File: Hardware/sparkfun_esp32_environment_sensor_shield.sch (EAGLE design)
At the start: 49 parts, among them J1 WEATHER_METER-WIND, J2 WEATHER_METER-RAIN, U1 BME280, U2 CCS811, U3 APDS-9301, U4 TVS Diode

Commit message: Feedback from review
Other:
- note added: "APDS-9301 - Luminosity (Lux)"
- note added: "APDS-9301 ===== VDD Range: 2.7-3.6V Max Current: 0.6mA"
- note added: "JP3 sets the I2C address of the APDS-9301 Open (both) - 0x51 High - 0x71 Low - 0x91"
- note removed: "JP3 sets the I2C address of the TSL2561 Open (both) - 0x39 High - 0x49 Low - 0x29"
- note removed: "TSL2561 - Luminosity (Lux)"
- note removed: "TSL2561 ===== VDD Range: 2.7-3.6V Max Current: 0.6mA"
- moved on the sheet: C6
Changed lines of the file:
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@@
 <sheet>
 <plain>
-<text x="104.14" y="119.38" size="1.27" layer="97">TSL2561
+<text x="104.14" y="119.38" size="1.27" layer="97">APDS-9301
 =====
 VDD Range: 2.7-3.6V
@@
 <wire x1="78.74" y1="76.2" x2="78.74" y2="132.08" width="0.254" layer="97" style="shortdash"/>
 <text x="0.762" y="131.318" size="2.54" layer="94" align="top-left">BME280 - Humidity, Pressure, Temp</text>
-<text x="79.502" y="131.318" size="2.54" layer="94" align="top-left">TSL2561 - Luminosity (Lux)</text>
+<text x="79.502" y="131.318" size="2.54" layer="94" align="top-left">APDS-9301 - Luminosity (Lux)</text>
 <text x="0.762" y="75.438" size="2.54" layer="94" align="top-left">Weather Meter - Rainfall, Wind Speed, Wind Direction</text>
 <wire x1="0" y1="25.4" x2="91.44" y2="25.4" width="0.254" layer="97" style="shortdash"/>
@@
 Closed - 0x76</text>
 <text x="81.28" y="81.28" size="1.27" layer="97" align="center-left">JP3 sets the I2C
-address of the TSL2561
-Open (both) - 0x39
-High - 0x49
-Low - 0x29</text>
+address of the APDS-9301
+Open (both) - 0x51
+High - 0x71
+Low - 0x91</text>
 <text x="111.76" y="157.48" size="1.27" layer="97" align="center-right">JP4 disconnects the on-
 board NTC thermistor,
@@
 <instance part="R14" gate="G$1" x="165.1" y="160.02" rot="R90"/>
 <instance part="SUPPLY18" gate="G$1" x="157.48" y="177.8"/>
-<instance part="C6" gate="G$1" x="139.7" y="116.84" rot="MR0"/>
-<instance part="SUPPLY17" gate="G$1" x="139.7" y="124.46"/>
-<instance part="GND15" gate="1" x="139.7" y="109.22"/>
+<instance part="C6" gate="G$1" x="139.7" y="114.3" rot="MR0"/>
+<instance part="SUPPLY17" gate="G$1" x="139.7" y="121.92"/>
+<instance part="GND15" gate="1" x="139.7" y="106.68"/>
 <instance part="SUPPLY1" gate="G$1" x="5.08" y="101.6"/>
 <instance part="R7" gate="G$1" x="91.44" y="111.76" rot="R90"/>
@@
 <pinref part="C6" gate="G$1" pin="2"/>
 <pinref part="GND15" gate="1" pin="GND"/>
-<wire x1="139.7" y1="111.76" x2="139.7" y2="114.3" width="0.1524" layer="91"/>
+<wire x1="139.7" y1="109.22" x2="139.7" y2="111.76" width="0.1524" layer="91"/>
 </segment>
 <segment>
@@
 <pinref part="C6" gate="G$1" pin="1"/>
 <pinref part="SUPPLY17" gate="G$1" pin="3.3V"/>
-<wire x1="139.7" y1="124.46" x2="139.7" y2="121.92" width="0.1524" layer="91"/>
-</segment>
-<segment>
+<wire x1="139.7" y1="121.92" x2="139.7" y2="119.38" width="0.1524" layer="91"/>
+</segment>
+<segment>

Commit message: Chg rev to 02
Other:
- note added: "02"
- note removed: "V01"
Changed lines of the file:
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@@
 to 4.7k pull-up
 resistors.</text>
-<text x="238.76" y="7.62" size="2.54" layer="94" align="center-left">V01</text>
+<text x="238.76" y="7.62" size="2.54" layer="94" align="center-left">02</text>
 <text x="170.18" y="7.62" size="2.54" layer="94" align="center-left">Jim Lindblom</text>
 <text x="119.38" y="20.32" size="1.27" layer="97" align="top-left">3-Pin temperature

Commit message: Fix issues from review
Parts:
- added FD3, FD4: FIDUCIAL1X2, SparkFun-Aesthetics:FIDUCIAL1X2
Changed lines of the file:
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@@
 <part name="LOGO3" library="SparkFun-Aesthetics" deviceset="SFE_LOGO_FLAME" device=".1_INCH"/>
 <part name="U3" library="SparkFun-Sensors" deviceset="APDS-9301" device="" value="APDS-9301"/>
+<part name="FD3" library="SparkFun-Aesthetics" deviceset="FIDUCIAL" device="1X2"/>
+<part name="FD4" library="SparkFun-Aesthetics" deviceset="FIDUCIAL" device="1X2"/>
 </parts>
 <sheets>
@@
 <instance part="LOGO3" gate="G$1" x="33.782" y="12.446"/>
 <instance part="U3" gate="G$1" x="116.84" y="99.06"/>
+<instance part="FD3" gate="G$1" x="236.22" y="27.94"/>
+<instance part="FD4" gate="G$1" x="236.22" y="25.4"/>
 </instances>
 <busses>

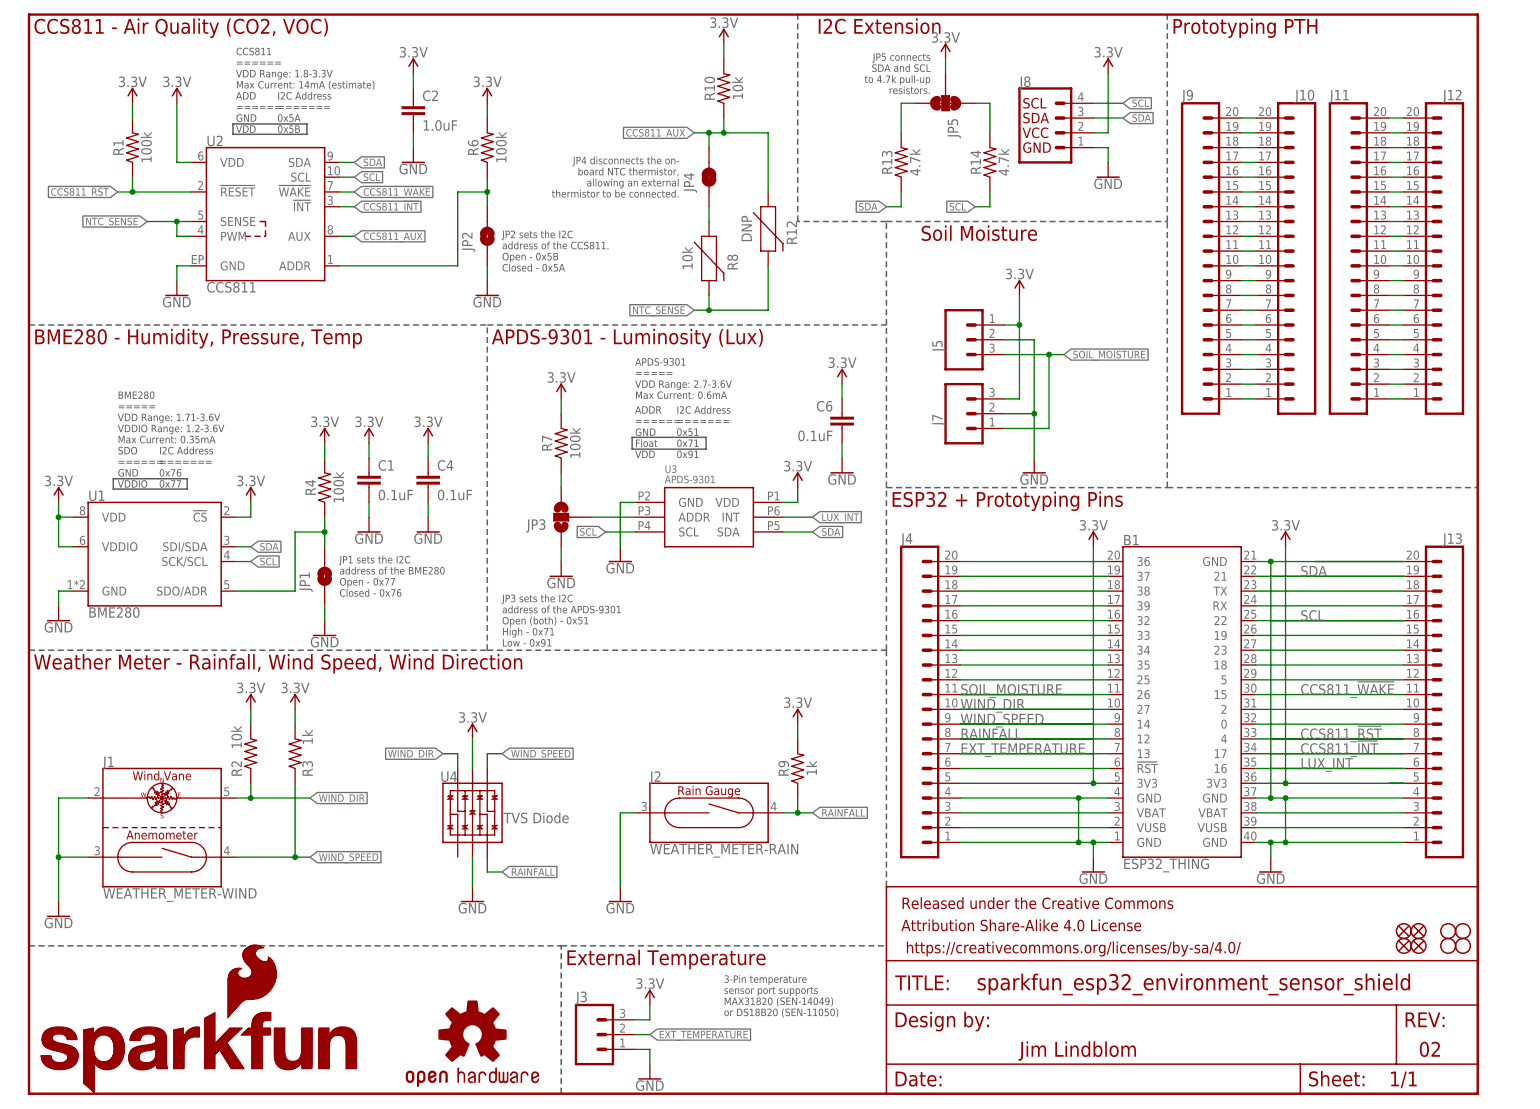
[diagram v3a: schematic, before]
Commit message: Changes after review of 02  - Change i2c addr info for apds-9301  - Change pin rain sensor is attached to  - Add debounce caps to rain sensor and anemometer  - Fix APDS-9301 footprint
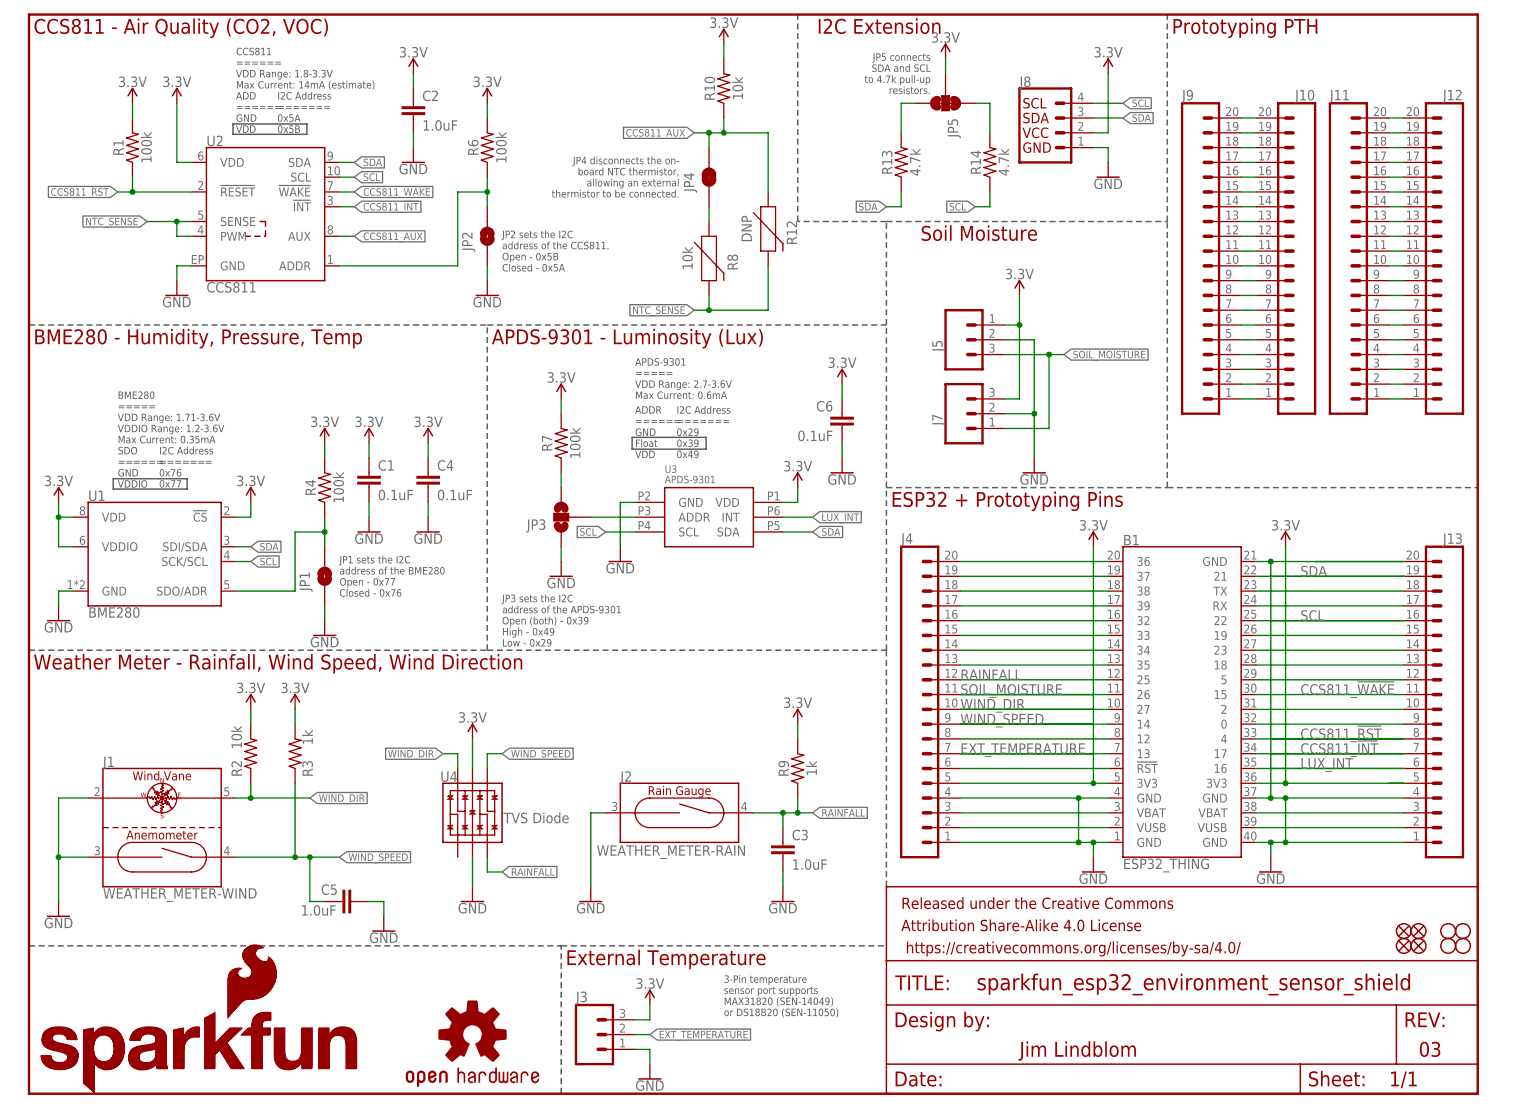
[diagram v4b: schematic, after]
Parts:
- added C3, C5: 1.0uF, SparkFun-Capacitors:1.0UF-0603-16V-10%
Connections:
- removed net N$9: B1.25, J4.12
- new net N$22: B1.12, J4.8
- net GND: now also C3.2, C5.2
- net RAINFALL: now also B1.25, C3.1, J4.12; no longer B1.12, J4.8
- net WIND_SPEED: now also C5.1
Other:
- note added: "03"
- note added: "I2C Address ======= 0x29 0x39 0x49"
- note added: "JP3 sets the I2C address of the APDS-9301 Open (both) - 0x39 High - 0x49 Low - 0x29"
- note removed: "02"
- note removed: "I2C Address ======= 0x51 0x71 0x91"
- note removed: "JP3 sets the I2C address of the APDS-9301 Open (both) - 0x51 High - 0x71 Low - 0x91"
- moved on the sheet: J2
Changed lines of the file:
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@@
 <part name="FD3" library="SparkFun-Aesthetics" deviceset="FIDUCIAL" device="1X2"/>
 <part name="FD4" library="SparkFun-Aesthetics" deviceset="FIDUCIAL" device="1X2"/>
+<part name="C3" library="SparkFun-Capacitors" deviceset="1.0UF" device="-0603-16V-10%" value="1.0uF"/>
+<part name="C5" library="SparkFun-Capacitors" deviceset="1.0UF" device="-0603-16V-10%" value="1.0uF"/>
+<part name="GND13" library="SparkFun-PowerSymbols" deviceset="GND" device=""/>
+<part name="GND20" library="SparkFun-PowerSymbols" deviceset="GND" device=""/>
 </parts>
 <sheets>
@@
 <text x="111.252" y="109.22" size="1.27" layer="97">I2C Address
 =======
-0x51
-0x71
-0x91</text>
+0x29
+0x39
+0x49</text>
 <text x="15.24" y="111.76" size="1.27" layer="97">BME280
 =====
@@
 <text x="81.28" y="81.28" size="1.27" layer="97" align="center-left">JP3 sets the I2C
 address of the APDS-9301
-Open (both) - 0x51
-High - 0x71
-Low - 0x91</text>
+Open (both) - 0x39
+High - 0x49
+Low - 0x29</text>
 <text x="111.76" y="157.48" size="1.27" layer="97" align="center-right">JP4 disconnects the on-
 board NTC thermistor,
@@
 to 4.7k pull-up
 resistors.</text>
-<text x="238.76" y="7.62" size="2.54" layer="94" align="center-left">02</text>
+<text x="238.76" y="7.62" size="2.54" layer="94" align="center-left">03</text>
 <text x="170.18" y="7.62" size="2.54" layer="94" align="center-left">Jim Lindblom</text>
 <text x="119.38" y="20.32" size="1.27" layer="97" align="top-left">3-Pin temperature
@@
 <instance part="SUPPLY11" gate="G$1" x="78.74" y="170.18"/>
 <instance part="JP4" gate="G$1" x="116.84" y="157.48" rot="R90"/>
-<instance part="J2" gate="G$1" x="116.84" y="48.26"/>
+<instance part="J2" gate="G$1" x="111.76" y="48.26" smashed="yes">
+<attribute name="VALUE" x="97.536" y="42.672" size="1.778" layer="96" font="vector" align="top-left"/>
+<attribute name="NAME" x="101.6" y="53.594" size="1.778" layer="95" font="vector"/>
+</instance>
 <instance part="J1" gate="G$1" x="22.86" y="48.26"/>
 <instance part="GND2" gate="1" x="5.08" y="30.48"/>
-<instance part="GND10" gate="1" x="101.6" y="33.02" rot="MR0"/>
+<instance part="GND10" gate="1" x="96.52" y="33.02" rot="MR0"/>
 <instance part="R9" gate="G$1" x="132.08" y="55.88" rot="R90"/>
 <instance part="H3" gate="G$1" x="246.38" y="27.94"/>
@@
 <instance part="FD3" gate="G$1" x="236.22" y="27.94"/>
 <instance part="FD4" gate="G$1" x="236.22" y="25.4"/>
+<instance part="C3" gate="G$1" x="129.54" y="40.64"/>
+<instance part="C5" gate="G$1" x="55.88" y="33.02" smashed="yes" rot="R90">
+<attribute name="NAME" x="53.086" y="35.941" size="1.778" layer="95" font="vector" rot="R180"/>
+<attribute name="VALUE" x="52.832" y="32.385" size="1.778" layer="96" font="vector" rot="R180"/>
+</instance>
+<instance part="GND13" gate="1" x="60.96" y="27.94" rot="MR0"/>
+<instance part="GND20" gate="1" x="129.54" y="33.02" rot="MR0"/>
 </instances>
 <busses>
@@
 <segment>
 <pinref part="J2" gate="G$1" pin="1"/>
-<wire x1="104.14" y1="48.26" x2="101.6" y2="48.26" width="0.1524" layer="91"/>
-<wire x1="101.6" y1="48.26" x2="101.6" y2="35.56" width="0.1524" layer="91"/>
+<wire x1="99.06" y1="48.26" x2="96.52" y2="48.26" width="0.1524" layer="91"/>
+<wire x1="96.52" y1="48.26" x2="96.52" y2="35.56" width="0.1524" layer="91"/>
 <pinref part="GND10" gate="1" pin="GND"/>
 </segment>
@@
 <wire x1="101.6" y1="101.6" x2="104.14" y2="101.6" width="0.1524" layer="91"/>
 </segment>
+<segment>
+<pinref part="C5" gate="G$1" pin="2"/>
+<pinref part="GND13" gate="1" pin="GND"/>
+<wire x1="58.42" y1="33.02" x2="60.96" y2="33.02" width="0.1524" layer="91"/>
+<wire x1="60.96" y1="33.02" x2="60.96" y2="30.48" width="0.1524" layer="91"/>
+</segment>
+<segment>
+<pinref part="GND20" gate="1" pin="GND"/>
+<pinref part="C3" gate="G$1" pin="2"/>
+<wire x1="129.54" y1="35.56" x2="129.54" y2="38.1" width="0.1524" layer="91"/>
+</segment>
 </net>
 <net name="SCL" class="0">
@@
 <label x="134.62" y="48.26" size="1.27" layer="95" xref="yes"/>
 <pinref part="J2" gate="G$1" pin="2"/>
+<wire x1="124.46" y1="48.26" x2="129.54" y2="48.26" width="0.1524" layer="91"/>
+<pinref part="R9" gate="G$1" pin="1"/>
 <wire x1="129.54" y1="48.26" x2="132.08" y2="48.26" width="0.1524" layer="91"/>
-<pinref part="R9" gate="G$1" pin="1"/>
 <wire x1="132.08" y1="48.26" x2="132.08" y2="50.8" width="0.1524" layer="91"/>
 <junction x="132.08" y="48.26"/>
 <wire x1="134.62" y1="48.26" x2="132.08" y2="48.26" width="0.1524" layer="91"/>
-</segment>
-<segment>
-<pinref part="B1" gate="G$1" pin="12"/>
-<wire x1="160.02" y1="60.96" x2="182.88" y2="60.96" width="0.1524" layer="91"/>
-<pinref part="J4" gate="G$1" pin="8"/>
-<wire x1="160.02" y1="60.96" x2="185.42" y2="60.96" width="0.1524" layer="91"/>
-<label x="160.02" y="60.96" size="1.778" layer="95"/>
+<pinref part="C3" gate="G$1" pin="1"/>
+<wire x1="129.54" y1="45.72" x2="129.54" y2="48.26" width="0.1524" layer="91"/>
+<junction x="129.54" y="48.26"/>
 </segment>
 <segment>
@@
 <wire x1="78.74" y1="38.1" x2="81.28" y2="38.1" width="0.1524" layer="91"/>
 <label x="81.28" y="38.1" size="1.27" layer="95" xref="yes"/>
+</segment>
+<segment>
+<pinref part="B1" gate="G$1" pin="25"/>
+<pinref part="J4" gate="G$1" pin="12"/>
+<wire x1="160.02" y1="71.12" x2="185.42" y2="71.12" width="0.1524" layer="91"/>
+<label x="160.02" y="71.12" size="1.778" layer="95"/>
 </segment>
 </net>
@@
 <wire x1="45.72" y1="53.34" x2="45.72" y2="40.64" width="0.1524" layer="91"/>
 <junction x="45.72" y="40.64"/>
+<wire x1="53.34" y1="40.64" x2="48.26" y2="40.64" width="0.1524" layer="91"/>
+<label x="53.34" y="40.64" size="1.27" layer="95" xref="yes"/>
+<pinref part="C5" gate="G$1" pin="1"/>
 <wire x1="48.26" y1="40.64" x2="45.72" y2="40.64" width="0.1524" layer="91"/>
-<label x="48.26" y="40.64" size="1.27" layer="95" xref="yes"/>
+<wire x1="50.8" y1="33.02" x2="48.26" y2="33.02" width="0.1524" layer="91"/>
+<wire x1="48.26" y1="33.02" x2="48.26" y2="40.64" width="0.1524" layer="91"/>
+<junction x="48.26" y="40.64"/>
 </segment>
 <segment>
@@
 </segment>
 </net>
-<net name="N$9" class="0">
-<segment>
-<pinref part="B1" gate="G$1" pin="25"/>
-<pinref part="J4" gate="G$1" pin="12"/>
-<wire x1="160.02" y1="71.12" x2="185.42" y2="71.12" width="0.1524" layer="91"/>
-</segment>
-</net>
 <net name="N$10" class="0">
 <segment>
@@
 </segment>
 </net>
+<net name="N$22" class="0">
+<segment>
+<pinref part="J4" gate="G$1" pin="8"/>
+<pinref part="B1" gate="G$1" pin="12"/>
+<wire x1="160.02" y1="60.96" x2="185.42" y2="60.96" width="0.1524" layer="91"/>
+</segment>
+</net>

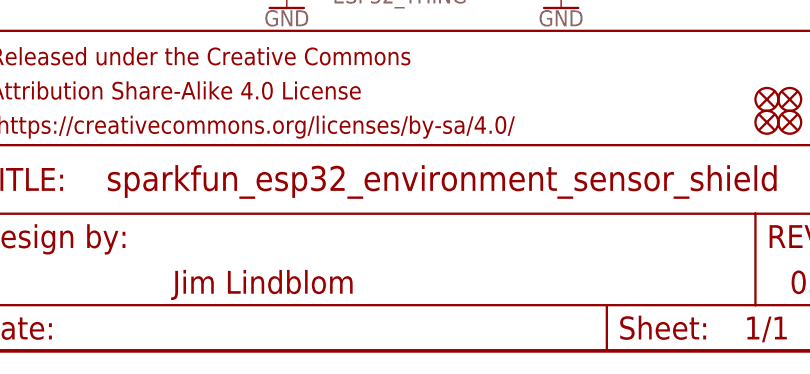
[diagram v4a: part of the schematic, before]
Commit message: Minor cosmetic changes from review
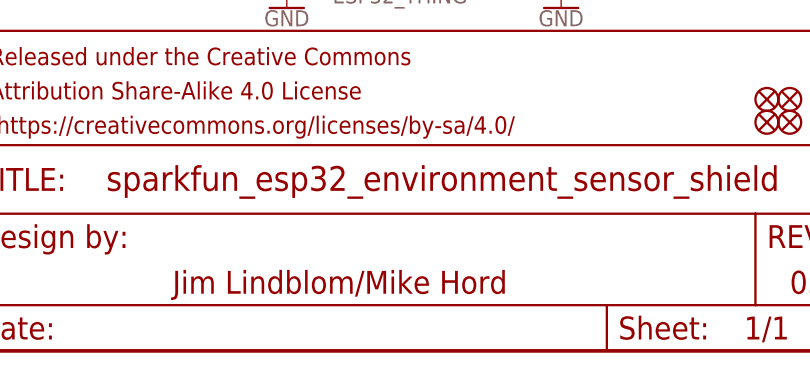
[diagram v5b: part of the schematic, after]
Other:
- note added: "Jim Lindblom/Mike Hord"
- note removed: "Jim Lindblom"
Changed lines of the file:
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@@
 resistors.</text>
 <text x="238.76" y="7.62" size="2.54" layer="94" align="center-left">03</text>
-<text x="170.18" y="7.62" size="2.54" layer="94" align="center-left">Jim Lindblom</text>
+<text x="170.18" y="7.62" size="2.54" layer="94" align="center-left">Jim Lindblom/Mike Hord</text>
 <text x="119.38" y="20.32" size="1.27" layer="97" align="top-left">3-Pin temperature
 sensor port supports

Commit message: Changes from review
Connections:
- removed net N$10: B1.35, J4.13
- new net N$9: B1.27, J4.10
- net WIND_DIR: now also B1.35, J4.13; no longer B1.27, J4.10
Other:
- note added: "10"
- note removed: "03"
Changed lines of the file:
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@@
 to 4.7k pull-up
 resistors.</text>
-<text x="238.76" y="7.62" size="2.54" layer="94" align="center-left">03</text>
+<text x="238.76" y="7.62" size="2.54" layer="94" align="center-left">10</text>
 <text x="170.18" y="7.62" size="2.54" layer="94" align="center-left">Jim Lindblom/Mike Hord</text>
 <text x="119.38" y="20.32" size="1.27" layer="97" align="top-left">3-Pin temperature
@@
 </segment>
 <segment>
-<pinref part="B1" gate="G$1" pin="27"/>
-<wire x1="160.02" y1="66.04" x2="182.88" y2="66.04" width="0.1524" layer="91"/>
-<pinref part="J4" gate="G$1" pin="10"/>
-<wire x1="160.02" y1="66.04" x2="185.42" y2="66.04" width="0.1524" layer="91"/>
-<label x="160.02" y="66.04" size="1.778" layer="95"/>
-</segment>
-<segment>
 <wire x1="73.66" y1="58.42" x2="71.12" y2="58.42" width="0.1524" layer="91"/>
 <pinref part="U4" gate="U1" pin="IO4"/>
 <wire x1="73.66" y1="55.88" x2="73.66" y2="58.42" width="0.1524" layer="91"/>
 <label x="71.12" y="58.42" size="1.27" layer="95" rot="R180" xref="yes"/>
+</segment>
+<segment>
+<pinref part="B1" gate="G$1" pin="35"/>
+<pinref part="J4" gate="G$1" pin="13"/>
+<wire x1="160.02" y1="73.66" x2="185.42" y2="73.66" width="0.1524" layer="91"/>
+<label x="160.02" y="73.66" size="1.778" layer="95"/>
 </segment>
 </net>
@@
 </segment>
 </net>
-<net name="N$10" class="0">
-<segment>
-<pinref part="B1" gate="G$1" pin="35"/>
-<pinref part="J4" gate="G$1" pin="13"/>
-<wire x1="160.02" y1="73.66" x2="185.42" y2="73.66" width="0.1524" layer="91"/>
-</segment>
-</net>
 <net name="N$11" class="0">
 <segment>
@@
 </segment>
 </net>
+<net name="N$9" class="0">
+<segment>
+<pinref part="J4" gate="G$1" pin="10"/>
+<pinref part="B1" gate="G$1" pin="27"/>
+<wire x1="160.02" y1="66.04" x2="185.42" y2="66.04" width="0.1524" layer="91"/>
+</segment>
+</net>
